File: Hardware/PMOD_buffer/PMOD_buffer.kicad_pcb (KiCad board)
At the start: 2 copper layers, 42 parts, among them J1 Conn_Coaxial, J2 Conn_Coaxial, J3 Conn_Coaxial, J4 Conn_Coaxial, J5 Conn_Coaxial, J6 Conn_Coaxial, J7 Conn_Coaxial, J8 Conn_Coaxial, J9 Conn_02x06_Top_Bottom, U1 74LVC04AT14-13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

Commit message: Routing Board
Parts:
- added H1: MountingHole_Pad, _tim-Mounting-Holes:4-40_Hole_Pad, F.Cu at (43.9, 41.4)
- added H2: MountingHole_Pad, _tim-Mounting-Holes:4-40_Hole_Pad, F.Cu at (43.9, 80.5)
- added H3: MountingHole_Pad, _tim-Mounting-Holes:4-40_Hole_Pad, F.Cu at (111.0, 80.5)
- added H4: MountingHole_Pad, _tim-Mounting-Holes:4-40_Hole_Pad, F.Cu at (111.0, 41.4)
- moved U3 64.6 mm to (59.9, 68.3), turned to 90 degrees
- moved R14 63.0 mm to (56.8, 62.5), turned to 90 degrees
- moved R13 50.3 mm to (62.0, 74.2), turned to -90 degrees
- moved R7 47.7 mm to (97.5, 56.6), turned to -90 degrees
- moved R15 47.7 mm to (58.8, 62.5), turned to 90 degrees
- moved U2 47.5 mm to (95.5, 50.8), turned to 90 degrees
- moved R16 47.5 mm to (60.8, 62.5), turned to 90 degrees
- moved R18 47.2 mm to (57.9, 74.2), turned to -90 degrees
- moved R10 46.9 mm to (96.5, 45.0), turned to 90 degrees
- moved C2 45.4 mm to (98.6, 45.0), turned to 90 degrees
- moved R9 44.4 mm to (94.5, 45.0), turned to 90 degrees
- moved R17 44.2 mm to (59.9, 74.2), turned to -90 degrees
- moved U4 43.4 mm to (95.5, 68.6), turned to 90 degrees
- moved R8 42.1 mm to (92.5, 45.0), turned to 90 degrees
- moved R12 42.0 mm to (93.5, 56.6), turned to -90 degrees
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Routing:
- net PMOD_ja_2: track 0.00 -> 84.0 mm, vias 0 -> 1
- net PMOD_ja_1: track 0.00 -> 78.8 mm
- net PMOD_ja_4: track 0.00 -> 52.5 mm
- net PMOD_ja_8: track 0.00 -> 47.1 mm, vias 0 -> 1
- net PMOD_ja_3: track 0.00 -> 47.0 mm, vias 0 -> 1
- net PMOD_ja_10: track 0.00 -> 31.1 mm
- net PMOD_ja_9: track 0.00 -> 29.9 mm
- net PMOD_ja_7: track 0.00 -> 25.7 mm, vias 0 -> 1
- net +3.3V: track 0.00 -> 21.1 mm, vias 0 -> 4
- net CH7_ja_7: track 0.00 -> 17.1 mm
- net CH3_ja_3: track 0.00 -> 17.1 mm
- net CH1_ja_1: track 0.00 -> 16.6 mm
- net CH5_ja_5: track 0.00 -> 15.9 mm
- net CH0_ja_0: track 0.00 -> 14.7 mm
- net CH2_ja_2: track 0.00 -> 14.7 mm
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- added copper zone on In1.Cu, net +3.3V
- added copper zone on B.Cu, net GND
- added copper zone on F.Cu, net GND
- added copper zone on In2.Cu, net GND
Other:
- board outline added: 73.7 x 45.7 mm
- copper layers 2 -> 4
- board text added: "CH0"
- board text added: "CH1"
- board text added: "CH2"
- board text added: "CH3"
- board text added: "CH4"
- board text added: "CH5"
- board text added: "CH6"
- board text added: "CH7"
- board text added: "G"
- board text added: "V"

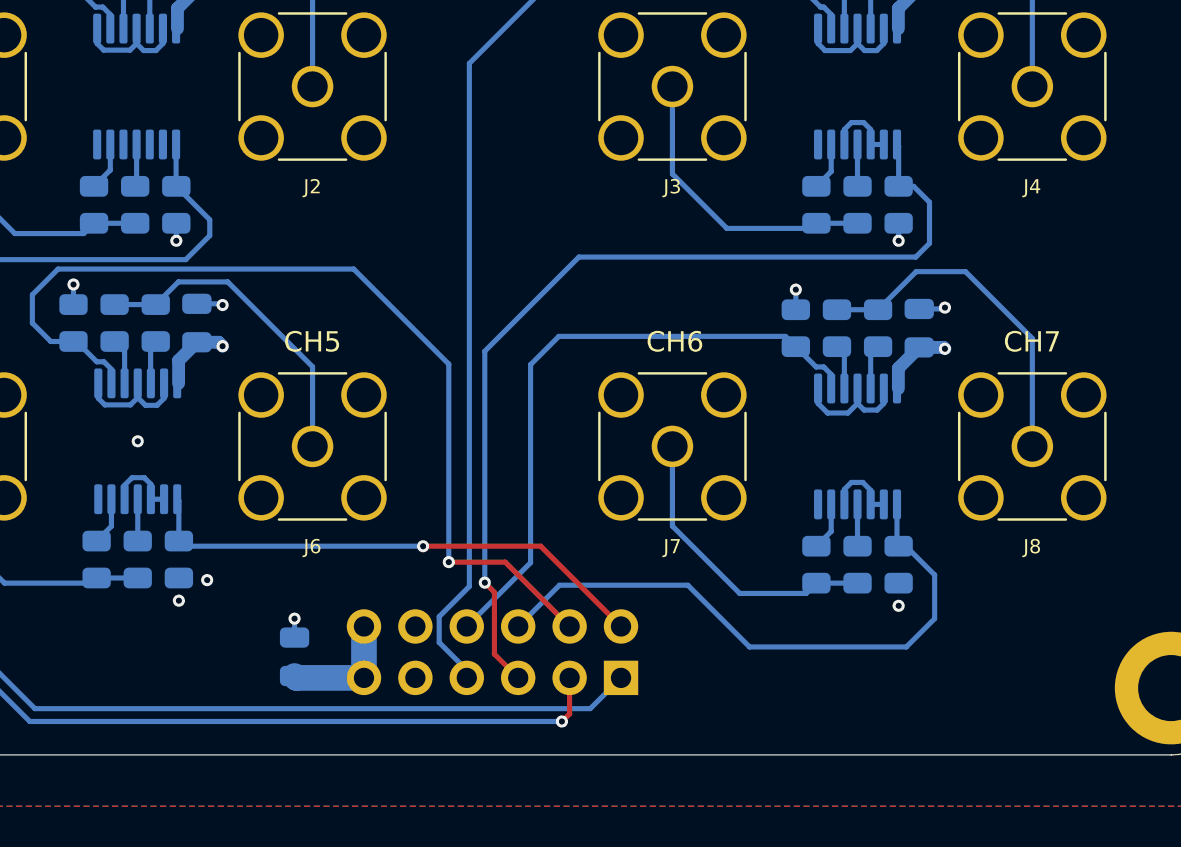
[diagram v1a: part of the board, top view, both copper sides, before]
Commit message: Updating PMOD Buffer BOM
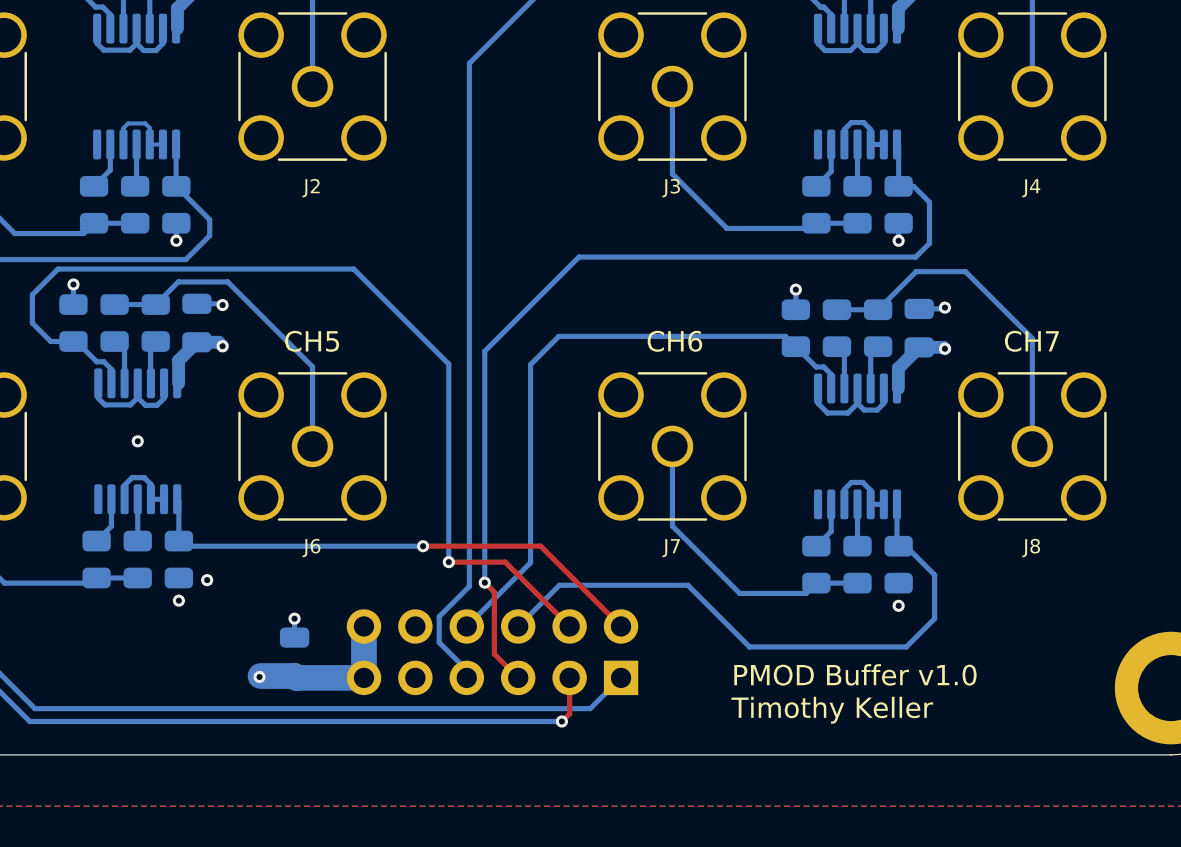
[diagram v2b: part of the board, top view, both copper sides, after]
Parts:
- J1, J2, J3, J4, J5, J6, J7, J8: value Conn_Coaxial -> RF2-152-T-00-50-G-HDW
- J9: value Conn_02x06_Top_Bottom -> 77313-101-12LF
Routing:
- net +3.3V: track 21.1 -> 40.6 mm, vias 4 -> 5
- net Net-(U1-Pad2): track 0.00 -> 3.76 mm
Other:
- board text added: "${TITLE} ${REVISION} ${COMMENT1}"
- board text added: "1"
- board text added: "4"
- board text added: "7"

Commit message: Generating Gerbers for Buffer
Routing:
- net GND: vias 15 -> 38
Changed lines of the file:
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@@
 			(outputformat 1)
 			(mirror no)
-			(drillshape 1)
+			(drillshape 0)
 			(scaleselection 1)
-			(outputdirectory "")
+			(outputdirectory "${PROJECTNAME}_${REVISION}_Gerbers/")
 		)
 	)
@@
 			(size 1.7 1.7)
 			(drill 1)
-			(layers "F&B.Cu" "*.Mask")
+			(layers "*.Cu" "*.Mask")
 			(remove_unused_layers no)
 			(net 11 "PMOD_ja_1")
@@
 			(size 1.7 1.7)
 			(drill 1)
-			(layers "F&B.Cu" "*.Mask")
+			(layers "*.Cu" "*.Mask")
 			(remove_unused_layers no)
 			(net 15 "PMOD_ja_2")
@@
 			(size 1.7 1.7)
 			(drill 1)
-			(layers "F&B.Cu" "*.Mask")
+			(layers "*.Cu" "*.Mask")
 			(remove_unused_layers no)
 			(net 14 "PMOD_ja_3")
@@
 			(size 1.7 1.7)
 			(drill 1)
-			(layers "F&B.Cu" "*.Mask")
+			(layers "*.Cu" "*.Mask")
 			(remove_unused_layers no)
 			(net 17 "PMOD_ja_4")
@@
 			(size 1.7 1.7)
 			(drill 1)
-			(layers "F&B.Cu" "*.Mask")
+			(layers "*.Cu" "*.Mask")
 			(remove_unused_layers no)
 			(net 1 "GND")
@@
 			(size 1.7 1.7)
 			(drill 1)
-			(layers "F&B.Cu" "*.Mask")
+			(layers "*.Cu" "*.Mask")
 			(remove_unused_layers no)
 			(net 2 "+3.3V")
@@
 			(size 1.7 1.7)
 			(drill 1)
-			(layers "F&B.Cu" "*.Mask")
+			(layers "*.Cu" "*.Mask")
 			(remove_unused_layers no)
 			(net 12 "PMOD_ja_7")
@@
 			(size 1.7 1.7)
 			(drill 1)
-			(layers "F&B.Cu" "*.Mask")
+			(layers "*.Cu" "*.Mask")
 			(remove_unused_layers no)
 			(net 13 "PMOD_ja_8")
@@
 			(size 1.7 1.7)
 			(drill 1)
-			(layers "F&B.Cu" "*.Mask")
+			(layers "*.Cu" "*.Mask")
 			(remove_unused_layers no)
 			(net 18 "PMOD_ja_9")
@@
 			(size 1.7 1.7)
 			(drill 1)
-			(layers "F&B.Cu" "*.Mask")
+			(layers "*.Cu" "*.Mask")
 			(remove_unused_layers no)
 			(net 16 "PMOD_ja_10")
@@
 			(size 1.7 1.7)
 			(drill 1)
-			(layers "F&B.Cu" "*.Mask")
+			(layers "*.Cu" "*.Mask")
 			(remove_unused_layers no)
 			(net 1 "GND")
@@
 			(size 1.7 1.7)
 			(drill 1)
-			(layers "F&B.Cu" "*.Mask")
+			(layers "*.Cu" "*.Mask")
 			(remove_unused_layers no)
 			(net 2 "+3.3V")
@@
 	)
 	(via
+		(at 55.88 40.64)
+		(size 0.6)
+		(drill 0.3)
+		(layers "F.Cu" "B.Cu")
+		(free yes)
+		(net 1)
+	)
+	(via
+		(at 76.2 40.64)
+		(size 0.6)
+		(drill 0.3)
+		(layers "F.Cu" "B.Cu")
+		(free yes)
+		(net 1)
+	)
+	(via
+		(at 111.76 73.66)
+		(size 0.6)
+		(drill 0.3)
+		(layers "F.Cu" "B.Cu")
+		(free yes)
+		(net 1)
+	)
+	(via
+		(at 91.44 77.47)
+		(size 0.6)
+		(drill 0.3)
+		(layers "F.Cu" "B.Cu")
+		(free yes)
+		(net 1)
+	)
+	(via
 		(at 56.896 43.053)
 		(size 0.6)
@@
 	)
 	(via
+		(at 66.04 40.64)
+		(size 0.6)
+		(drill 0.3)
+		(layers "F.Cu" "B.Cu")
+		(free yes)
+		(net 1)
+	)
+	(via
 		(at 92.456 43.18)
 		(size 0.6)
@@
 	)
 	(via
+		(at 73.66 58.42)
+		(size 0.6)
+		(drill 0.3)
+		(layers "F.Cu" "B.Cu")
+		(free yes)
+		(net 1)
+	)
+	(via
+		(at 71.12 40.64)
+		(size 0.6)
+		(drill 0.3)
+		(layers "F.Cu" "B.Cu")
+		(free yes)
+		(net 1)
+	)
+	(via
 		(at 97.536 58.419988)
 		(size 0.6)
@@
 	)
 	(via
+		(at 111.76 60.96)
+		(size 0.6)
+		(drill 0.3)
+		(layers "F.Cu" "B.Cu")
+		(free yes)
+		(net 1)
+	)
+	(via
 		(at 56.769 60.579)
 		(size 0.6)
@@
 	)
 	(via
+		(at 62.23 78.74)
+		(size 0.6)
+		(drill 0.3)
+		(layers "F.Cu" "B.Cu")
+		(free yes)
+		(net 1)
+	)
+	(via
+		(at 78.74 58.42)
+		(size 0.6)
+		(drill 0.3)
+		(layers "F.Cu" "B.Cu")
+		(free yes)
+		(net 1)
+	)
+	(via
+		(at 111.76 55.88)
+		(size 0.6)
+		(drill 0.3)
+		(layers "F.Cu" "B.Cu")
+		(free yes)
+		(net 1)
+	)
+	(via
 		(at 64.135 44.069)
 		(size 0.6)
@@
 	)
 	(via
+		(at 86.36 40.64)
+		(size 0.6)
+		(drill 0.3)
+		(layers "F.Cu" "B.Cu")
+		(free yes)
+		(net 1)
+	)
+	(via
+		(at 96.52 40.64)
+		(size 0.6)
+		(drill 0.3)
+		(layers "F.Cu" "B.Cu")
+		(free yes)
+		(net 1)
+	)
+	(via
+		(at 111.76 50.8)
+		(size 0.6)
+		(drill 0.3)
+		(layers "F.Cu" "B.Cu")
+		(free yes)
+		(net 1)
+	)
+	(via
 		(at 92.456 60.833)
 		(size 0.6)
@@
 	)
 	(via
+		(at 91.44 40.64)
+		(size 0.6)
+		(drill 0.3)
+		(layers "F.Cu" "B.Cu")
+		(free yes)
+		(net 1)
+	)
+	(via
 		(at 63.373 75.184)
 		(size 0.6)
@@
 	)
 	(via
+		(at 96.52 77.47)
+		(size 0.6)
+		(drill 0.3)
+		(layers "F.Cu" "B.Cu")
+		(free yes)
+		(net 1)
+	)
+	(via
+		(at 50.8 40.64)
+		(size 0.6)
+		(drill 0.3)
+		(layers "F.Cu" "B.Cu")
+		(free yes)
+		(net 1)
+	)
+	(via
+		(at 43.18 76.2)
+		(size 0.6)
+		(drill 0.3)
+		(layers "F.Cu" "B.Cu")
+		(free yes)
+		(net 1)
+	)
+	(via
+		(at 58.42 78.74)
+		(size 0.6)
+		(drill 0.3)
+		(layers "F.Cu" "B.Cu")
+		(free yes)
+		(net 1)
+	)
+	(via
 		(at 99.822 61.722)
 		(size 0.6)
@@
 	)
 	(via
+		(at 93.98 77.47)
+		(size 0.6)
+		(drill 0.3)
+		(layers "F.Cu" "B.Cu")
+		(free yes)
+		(net 1)
+	)
+	(via
+		(at 60.96 40.64)
+		(size 0.6)
+		(drill 0.3)
+		(layers "F.Cu" "B.Cu")
+		(free yes)
+		(net 1)
+	)
+	(via
 		(at 97.536 76.454)
 		(size 0.6)
 		(drill 0.3)
+		(layers "F.Cu" "B.Cu")
+		(free yes)
+		(net 1)
+	)
+	(via
+		(at 101.6 40.64)
+		(size 0.6)
+		(drill 0.3)
+		(layers "F.Cu" "B.Cu")
+		(free yes)
+		(net 1)
+	)
+	(via
+		(at 81.28 40.64)
+		(size 0.6)
+		(drill 0.3)
